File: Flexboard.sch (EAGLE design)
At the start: 421 parts, among them U1 MK22FX512AVLQ12

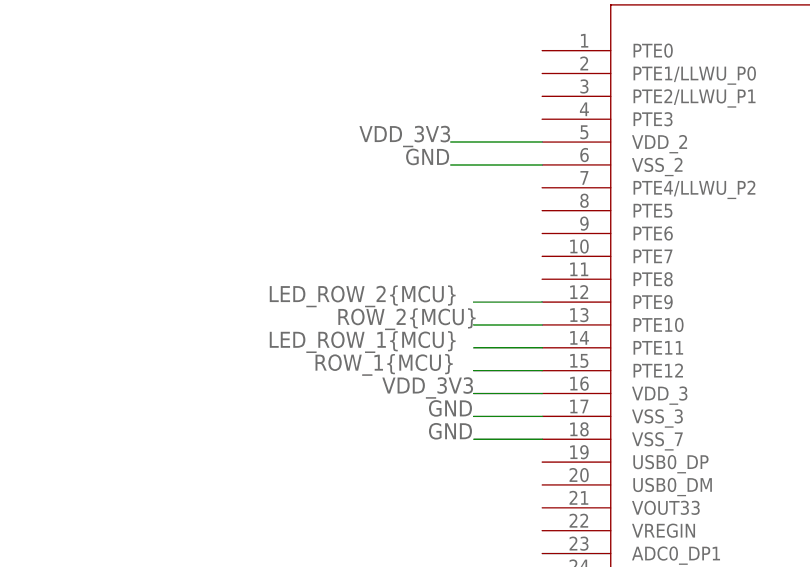
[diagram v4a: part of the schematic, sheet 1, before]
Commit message: All column and row traces routed to MCU
All column and row traces are connected to the MCU
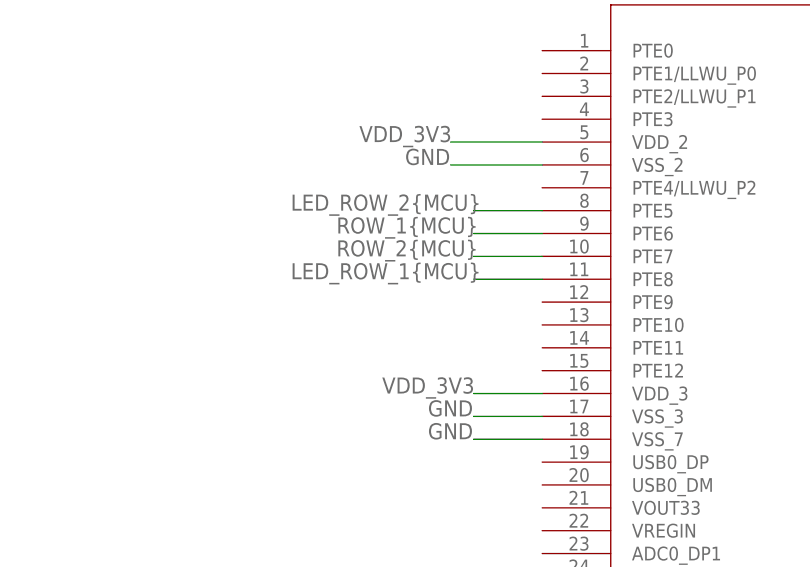
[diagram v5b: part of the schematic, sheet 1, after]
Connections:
- net LED_ROW_1{MCU}: now also U1A.PTE8; no longer U1A.PTE11
- net LED_ROW_2{MCU}: now also U1A.PTE5; no longer U1A.PTE9
- net ROW_1{MCU}: now also U1A.PTE6; no longer U1A.PTE12
- net ROW_2{MCU}: now also U1A.PTE7; no longer U1A.PTE10
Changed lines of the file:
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@@
 </segment>
 <segment>
-<pinref part="U1" gate="A" pin="PTE12"/>
-<wire x1="-48.26" y1="33.02" x2="-55.88" y2="33.02" width="0.1524" layer="91"/>
-<label x="-73.66" y="33.02" size="1.778" layer="95"/>
+<pinref part="U1" gate="A" pin="PTE6"/>
+<wire x1="-48.26" y1="48.26" x2="-55.88" y2="48.26" width="0.1524" layer="91"/>
+<label x="-71.12" y="48.26" size="1.778" layer="95"/>
 </segment>
 </net>
@@
 </segment>
 <segment>
-<pinref part="U1" gate="A" pin="PTE10"/>
-<wire x1="-48.26" y1="38.1" x2="-55.88" y2="38.1" width="0.1524" layer="91"/>
-<label x="-71.12" y="38.1" size="1.778" layer="95"/>
+<pinref part="U1" gate="A" pin="PTE7"/>
+<wire x1="-48.26" y1="45.72" x2="-55.88" y2="45.72" width="0.1524" layer="91"/>
+<label x="-71.12" y="45.72" size="1.778" layer="95"/>
 </segment>
 </net>
@@
 <net name="LED_ROW_2{MCU}" class="0">
 <segment>
-<pinref part="U1" gate="A" pin="PTE9"/>
-<wire x1="-48.26" y1="40.64" x2="-55.88" y2="40.64" width="0.1524" layer="91"/>
-<label x="-78.74" y="40.64" size="1.778" layer="95"/>
-</segment>
-<segment>
 <pinref part="SJ_MCU_LED_ROW2" gate="G$1" pin="2"/>
 <wire x1="58.42" y1="198.12" x2="66.04" y2="198.12" width="0.1524" layer="91"/>
 <label x="66.04" y="198.12" size="1.778" layer="95"/>
 </segment>
+<segment>
+<pinref part="U1" gate="A" pin="PTE5"/>
+<wire x1="-48.26" y1="50.8" x2="-55.88" y2="50.8" width="0.1524" layer="91"/>
+<label x="-76.2" y="50.8" size="1.778" layer="95"/>
+</segment>
 </net>
 <net name="LED_ROW_1{MCU}" class="0">
-<segment>
-<pinref part="U1" gate="A" pin="PTE11"/>
-<wire x1="-48.26" y1="35.56" x2="-55.88" y2="35.56" width="0.1524" layer="91"/>
-<label x="-78.74" y="35.56" size="1.778" layer="95"/>
-</segment>
 <segment>
 <pinref part="SJ_MCU_LED_ROW1" gate="G$1" pin="2"/>
@@
 <label x="66.04" y="205.74" size="1.778" layer="95"/>
 </segment>
+<segment>
+<pinref part="U1" gate="A" pin="PTE8"/>
+<wire x1="-48.26" y1="43.18" x2="-55.88" y2="43.18" width="0.1524" layer="91"/>
+<label x="-76.2" y="43.18" size="1.778" layer="95"/>
+</segment>
 </net>

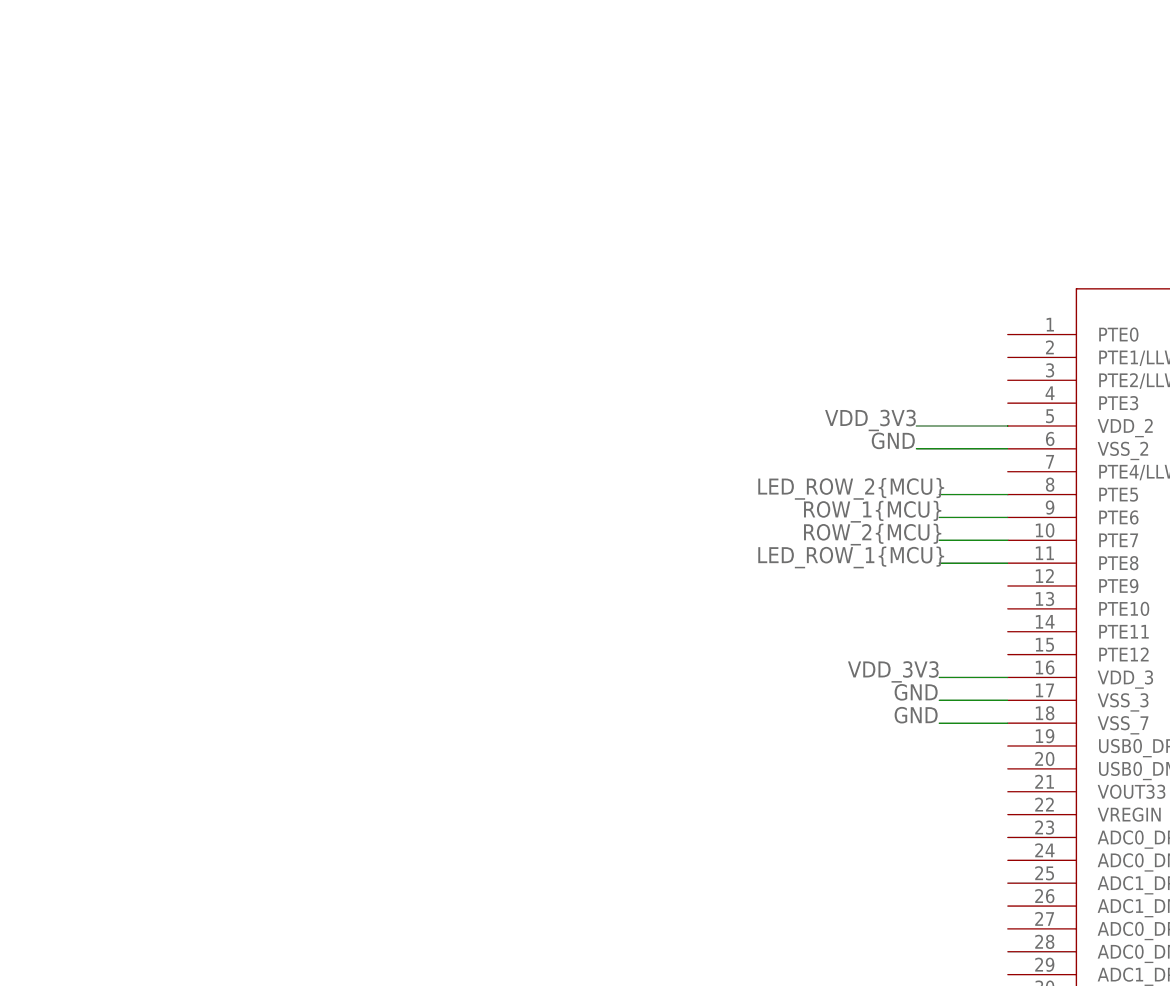
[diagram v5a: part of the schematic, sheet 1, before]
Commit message: Added usb to MCU and routed power planes
Added board wide power and ground planes, as well as USB traces to kinetis MCU.

Signed-off-by: Daniel DeGrasse <daniel@degrasse.com>
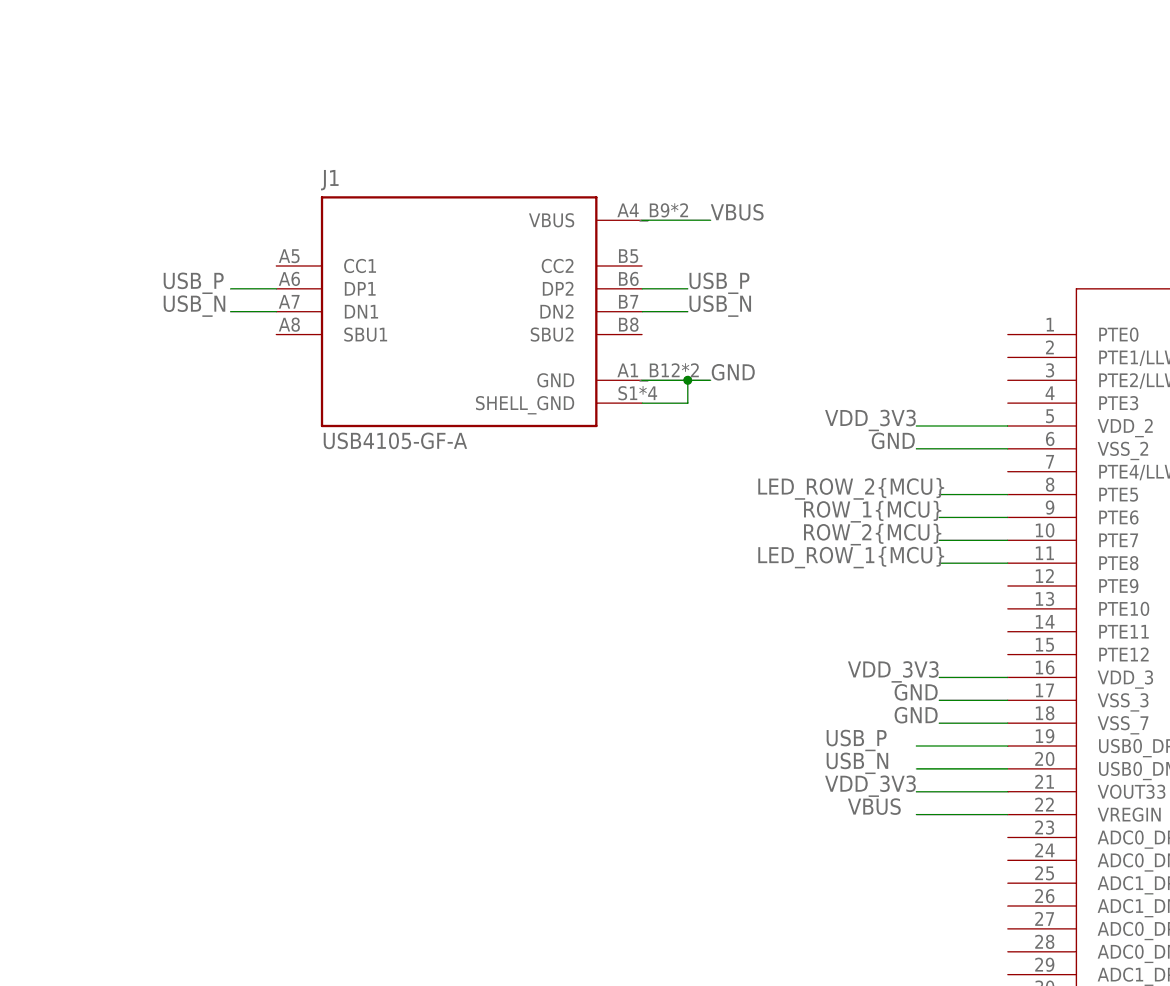
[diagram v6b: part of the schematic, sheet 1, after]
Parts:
- added J1: USB4105-GF-A, USB4105-GF-A:USB4105-GF-A
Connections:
- new net USB_N: J1.DN1, J1.DN2, U1A.USB0_DM
- new net USB_P: J1.DP1, J1.DP2, U1A.USB0_DP
- new net VBUS: J1.VBUS, U1A.VREGIN
- net GND: now also J1.GND, J1.SHELL_GND
- net VDD_3V3: now also U1A.VOUT33
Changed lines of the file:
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@@
 <part name="SJ_MCU_LED_COL23" library="SparkFun-Jumpers" deviceset="JUMPER-SMT_2_NC_TRACE" device="_NO-SILK" package3d_urn="urn:adsk.eagle:package:39286/1"/>
 <part name="SJ_MCU_LED_COL24" library="SparkFun-Jumpers" deviceset="JUMPER-SMT_2_NC_TRACE" device="_NO-SILK" package3d_urn="urn:adsk.eagle:package:39286/1"/>
+<part name="J1" library="USB4105-GF-A" deviceset="USB4105-GF-A" device=""/>
 </parts>
 <sheets>
@@
 <attribute name="NAME" x="-104.14" y="124.968" size="1.778" layer="95" font="vector" align="center"/>
 </instance>
+<instance part="J1" gate="G$1" x="-109.22" y="71.12" smashed="yes">
+<attribute name="NAME" x="-124.46" y="85.09" size="1.778" layer="95"/>
+<attribute name="VALUE" x="-124.46" y="55.88" size="1.778" layer="96"/>
+</instance>
 </instances>
 <busses>
@@
 <label x="101.6" y="-116.84" size="1.778" layer="95"/>
 </segment>
+<segment>
+<pinref part="U1" gate="A" pin="VOUT33"/>
+<wire x1="-48.26" y1="17.78" x2="-58.42" y2="17.78" width="0.1524" layer="91"/>
+<label x="-68.58" y="17.78" size="1.778" layer="95"/>
+</segment>
 </net>
 <net name="GND" class="0">
@@
 <label x="101.6" y="-119.38" size="1.778" layer="95"/>
 </segment>
+<segment>
+<pinref part="J1" gate="G$1" pin="GND"/>
+<wire x1="-88.9" y1="63.5" x2="-83.82" y2="63.5" width="0.1524" layer="91"/>
+<pinref part="J1" gate="G$1" pin="SHELL_GND"/>
+<wire x1="-83.82" y1="63.5" x2="-81.28" y2="63.5" width="0.1524" layer="91"/>
+<wire x1="-88.9" y1="60.96" x2="-83.82" y2="60.96" width="0.1524" layer="91"/>
+<wire x1="-83.82" y1="60.96" x2="-83.82" y2="63.5" width="0.1524" layer="91"/>
+<junction x="-83.82" y="63.5"/>
+<label x="-81.28" y="63.5" size="1.778" layer="95"/>
+</segment>
 </net>
 <net name="ROW_5{SB}" class="0">
@@
 </segment>
 </net>
+<net name="USB_P" class="0">
+<segment>
+<pinref part="U1" gate="A" pin="USB0_DP"/>
+<wire x1="-48.26" y1="22.86" x2="-58.42" y2="22.86" width="0.1524" layer="91"/>
+<label x="-68.58" y="22.86" size="1.778" layer="95"/>
+</segment>
+<segment>
+<pinref part="J1" gate="G$1" pin="DP2"/>
+<wire x1="-88.9" y1="73.66" x2="-83.82" y2="73.66" width="0.1524" layer="91"/>
+<label x="-83.82" y="73.66" size="1.778" layer="95"/>
+</segment>
+<segment>
+<pinref part="J1" gate="G$1" pin="DP1"/>
+<wire x1="-129.54" y1="73.66" x2="-134.62" y2="73.66" width="0.1524" layer="91"/>
+<label x="-142.24" y="73.66" size="1.778" layer="95"/>
+</segment>
+</net>
+<net name="USB_N" class="0">
+<segment>
+<pinref part="U1" gate="A" pin="USB0_DM"/>
+<wire x1="-48.26" y1="20.32" x2="-58.42" y2="20.32" width="0.1524" layer="91"/>
+<label x="-68.58" y="20.32" size="1.778" layer="95"/>
+</segment>
+<segment>
+<pinref part="J1" gate="G$1" pin="DN2"/>
+<wire x1="-88.9" y1="71.12" x2="-83.82" y2="71.12" width="0.1524" layer="91"/>
+<label x="-83.82" y="71.12" size="1.778" layer="95"/>
+</segment>
+<segment>
+<pinref part="J1" gate="G$1" pin="DN1"/>
+<wire x1="-129.54" y1="71.12" x2="-134.62" y2="71.12" width="0.1524" layer="91"/>
+<label x="-142.24" y="71.12" size="1.778" layer="95"/>
+</segment>
+</net>
+<net name="VBUS" class="0">
+<segment>
+<pinref part="U1" gate="A" pin="VREGIN"/>
+<wire x1="-48.26" y1="15.24" x2="-58.42" y2="15.24" width="0.1524" layer="91"/>
+<label x="-66.04" y="15.24" size="1.778" layer="95"/>
+</segment>
+<segment>
+<pinref part="J1" gate="G$1" pin="VBUS"/>
+<wire x1="-88.9" y1="81.28" x2="-81.28" y2="81.28" width="0.1524" layer="91"/>
+<label x="-81.28" y="81.28" size="1.778" layer="95"/>
+</segment>
+</net>

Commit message: Added decoupling capacitors around the mcu
added power caps to MCU, 1uF and 100nF

Signed-off-by: Daniel DeGrasse <daniel@degrasse.com>
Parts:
- added C1: 1000pF, C1206C102K1RACAUTO:C1206C102K1RACAUTO
- added C2, C3, C4, C8: 1uF, GCM31MR71H105KA55L:GCM31MR71H105KA55L
- added C5, C6, C7, C9: 100nF, C1206C104K5RAC7800:C1206C104K5RAC7800
- added R1: 10k, CRGCQ1206J10K:CRGCQ1206J10K
- added SW1: 1825910-7, 1825910-7:1825910-7
- added U$1: GRPB052VWQS-RC, GRPB052VWQS-RC:GRPB052VWQS-RC
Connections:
- removed net JTAG_TRST: U1A.PTA5
- new net EXTAL: U1A.PTA18
- new net EXTAL32: U1A.EXTAL32
- new net NMI: U1A.PTA4/LLWU_P3
- new net XTAL: U1B.PTA19
- new net XTAL32: U1A.XTAL32
- net COL_18{MCU}: now also U1A.PTA14; no longer U1A.PTA13/LLWU_P4
- net COL_19{MCU}: now also U1A.PTA12; no longer U1A.PTA11
- net COL_20{MCU}: now also U1A.PTA10; no longer U1A.PTA9
- net COL_21{MCU}: now also U1A.PTA8; no longer U1A.PTA7
- net COL_22{MCU}: now also U1A.PTA6; no longer U1A.PTA4/LLWU_P3
- net GND: now also C1.2, C2.2, C3.2, C4.2, C5.1, C6.1, C7.1, C8.2, C9.1, SW1.3, SW1.4, U$1.GND, U$1.GND2, U1A.VREFL, U1A.VSSA
- net JTAG_TCLK/SWD_CLK: now also U$1.TCK
- net JTAG_TDI: now also U$1.TDI
- net JTAG_TDO/TRACE_SWO: now also U$1.TDO
- net JTAG_TMS/SWD_DIO: now also U$1.TMS
- net LED_COL_18{MCU}: now also U1A.PTA13/LLWU_P4; no longer U1A.PTA12
- net LED_COL_19{MCU}: now also U1A.PTA11; no longer U1A.PTA10
- net LED_COL_20{MCU}: now also U1A.PTA9; no longer U1A.PTA8
- net LED_COL_21{MCU}: now also U1A.PTA7; no longer U1A.PTA6
- net RESET: now also C1.1, R1.1, SW1.1, SW1.2, U$1.NRESET
- net VDD_3V3: now also C2.1, C3.1, C4.1, C5.2, C6.2, C7.2, C8.1, C9.2, R1.2, U$1.VCC, U1A.VBAT, U1A.VDDA, U1A.VREFH
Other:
- note added: "JTAG"
- note added: "MCU"
- note added: "Solder Bridges"
- note added: "USB"

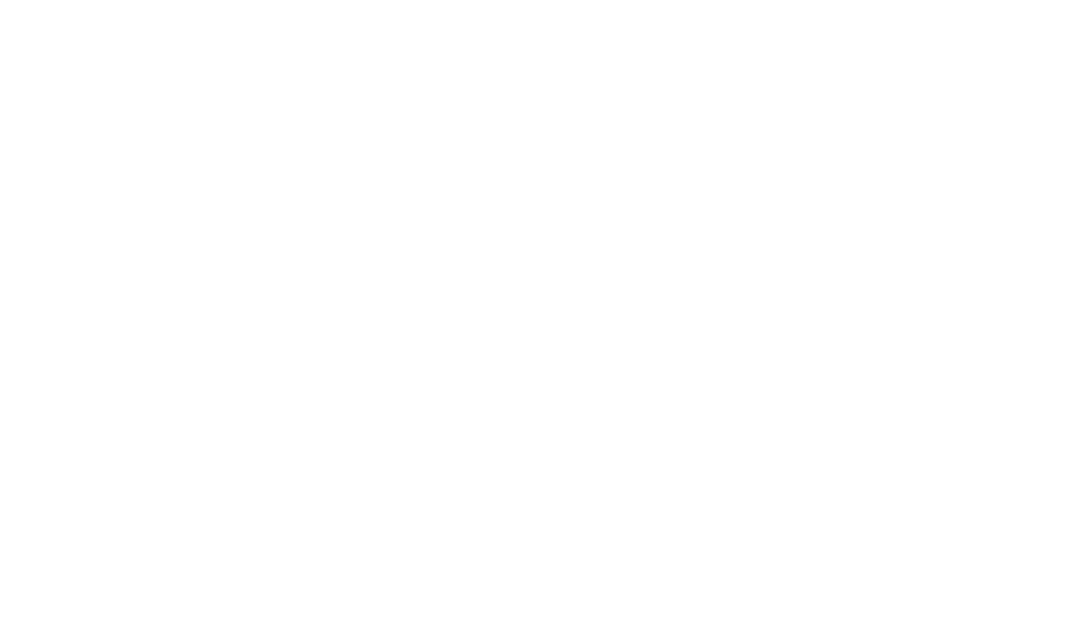
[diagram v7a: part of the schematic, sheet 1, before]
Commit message: added oscillators to design
added 8MHz and 32KHz crystals to design. Still need to add capacitors
and resistors for USB 5V as well as DP/DN

Signed-off-by: Daniel DeGrasse <daniel@degrasse.com>
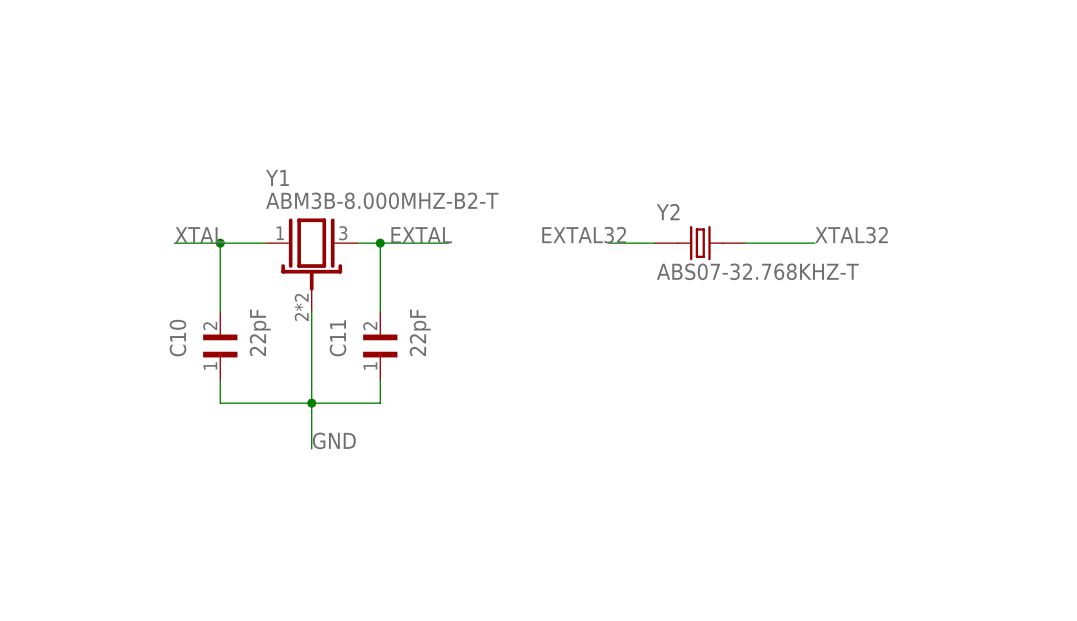
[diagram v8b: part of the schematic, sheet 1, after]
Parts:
- added C10, C11: 22pF, C1206C220JGGAC7800:C1206C220JGGAC7800
- added Y1: ABM3B-8.000MHZ-B2-T, ABM3B-8.000MHZ-B2-T:ABM3B-8.000MHZ-B2-T
- added Y2: ABS07-32.768KHZ-T, ABS07-32.768KHZ-T:ABS07-32.768KHZ-T
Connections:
- net EXTAL: now also C11.2, Y1.3
- net EXTAL32: now also Y2.1
- net GND: now also C10.1, C11.1, Y1.GND
- net XTAL: now also C10.2, Y1.1
- net XTAL32: now also Y2.2
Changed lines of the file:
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@@
 <part name="C8" library="GCM31MR71H105KA55L" deviceset="GCM31MR71H105KA55L" device="" value="1uF"/>
 <part name="C9" library="C1206C104K5RAC7800" deviceset="C1206C104K5RAC7800" device="" value="100nF"/>
+<part name="Y1" library="ABM3B-8.000MHZ-B2-T" deviceset="ABM3B-8.000MHZ-B2-T" device=""/>
+<part name="C10" library="C1206C220JGGAC7800" deviceset="C1206C220JGGAC7800" device="" value="22pF"/>
+<part name="C11" library="C1206C220JGGAC7800" deviceset="C1206C220JGGAC7800" device="" value="22pF"/>
+<part name="Y2" library="ABS07-32.768KHZ-T" deviceset="ABS07-32.768KHZ-T" device=""/>
 </parts>
 <sheets>
@@
 <attribute name="NAME" x="102.86906875" y="116.84" size="1.77843125" layer="95" rot="R90"/>
 <attribute name="VALUE" x="111.76848125" y="116.84" size="1.78096875" layer="96" rot="R90"/>
+</instance>
+<instance part="Y1" gate="G$1" x="220.98" y="15.24" smashed="yes">
+<attribute name="NAME" x="215.9" y="21.59" size="1.78073125" layer="95"/>
+<attribute name="VALUE" x="215.9" y="19.05" size="1.78303125" layer="96"/>
+</instance>
+<instance part="C10" gate="G$1" x="210.82" y="2.54" smashed="yes" rot="R90">
+<attribute name="NAME" x="207.00906875" y="2.54" size="1.77843125" layer="95" rot="R90"/>
+<attribute name="VALUE" x="215.90848125" y="2.54" size="1.78096875" layer="96" rot="R90"/>
+</instance>
+<instance part="C11" gate="G$1" x="228.6" y="2.54" smashed="yes" rot="R90">
+<attribute name="NAME" x="224.78906875" y="2.54" size="1.77843125" layer="95" rot="R90"/>
+<attribute name="VALUE" x="233.68848125" y="2.54" size="1.78096875" layer="96" rot="R90"/>
+</instance>
+<instance part="Y2" gate="G$1" x="264.16" y="15.24" smashed="yes">
+<attribute name="NAME" x="259.325690625" y="17.78436875" size="1.781059375" layer="95"/>
+<attribute name="VALUE" x="259.323540625" y="11.167190625" size="1.78185" layer="96"/>
 </instance>
 </instances>
@@
 <junction x="93.98" y="109.22"/>
 </segment>
+<segment>
+<pinref part="C10" gate="G$1" pin="1"/>
+<wire x1="210.82" y1="0" x2="210.82" y2="-2.54" width="0.1524" layer="91"/>
+<wire x1="210.82" y1="-2.54" x2="220.98" y2="-2.54" width="0.1524" layer="91"/>
+<pinref part="C11" gate="G$1" pin="1"/>
+<wire x1="220.98" y1="-2.54" x2="228.6" y2="-2.54" width="0.1524" layer="91"/>
+<wire x1="228.6" y1="-2.54" x2="228.6" y2="0" width="0.1524" layer="91"/>
+<pinref part="Y1" gate="G$1" pin="GND"/>
+<wire x1="220.98" y1="7.62" x2="220.98" y2="-2.54" width="0.1524" layer="91"/>
+<junction x="220.98" y="-2.54"/>
+<wire x1="220.98" y1="-2.54" x2="220.98" y2="-7.62" width="0.1524" layer="91"/>
+<label x="220.98" y="-7.62" size="1.778" layer="95"/>
+</segment>
 </net>
 <net name="ROW_5{SB}" class="0">
@@
 <label x="144.78" y="-10.16" size="1.778" layer="95"/>
 </segment>
+<segment>
+<pinref part="Y2" gate="G$1" pin="1"/>
+<wire x1="259.08" y1="15.24" x2="254" y2="15.24" width="0.1524" layer="91"/>
+<label x="246.38" y="15.24" size="1.778" layer="95"/>
+</segment>
 </net>
 <net name="XTAL32" class="0">
@@
 <label x="144.78" y="-12.7" size="1.778" layer="95"/>
 </segment>
+<segment>
+<pinref part="Y2" gate="G$1" pin="2"/>
+<wire x1="269.24" y1="15.24" x2="276.86" y2="15.24" width="0.1524" layer="91"/>
+<label x="276.86" y="15.24" size="1.778" layer="95"/>
+</segment>
 </net>
 <net name="EXTAL" class="0">
@@
 <label x="144.78" y="68.58" size="1.778" layer="95"/>
 </segment>
+<segment>
+<pinref part="Y1" gate="G$1" pin="3"/>
+<wire x1="226.06" y1="15.24" x2="228.6" y2="15.24" width="0.1524" layer="91"/>
+<label x="229.616" y="15.24" size="1.778" layer="95"/>
+<pinref part="C11" gate="G$1" pin="2"/>
+<wire x1="228.6" y1="15.24" x2="236.22" y2="15.24" width="0.1524" layer="91"/>
+<wire x1="228.6" y1="7.62" x2="228.6" y2="15.24" width="0.1524" layer="91"/>
+<junction x="228.6" y="15.24"/>
+</segment>
 </net>
 <net name="XTAL" class="0">
@@
 <label x="-15.24" y="-60.96" size="1.778" layer="95"/>
 </segment>
-</net>
+<segment>
+<pinref part="Y1" gate="G$1" pin="1"/>
+<wire x1="215.9" y1="15.24" x2="210.82" y2="15.24" width="0.1524" layer="91"/>
+<label x="205.74" y="15.24" size="1.778" layer="95"/>
+<pinref part="C10" gate="G$1" pin="2"/>
+<wire x1="210.82" y1="15.24" x2="205.74" y2="15.24" width="0.1524" layer="91"/>
+<wire x1="210.82" y1="7.62" x2="210.82" y2="15.24" width="0.1524" layer="91"/>
+<junction x="210.82" y="15.24"/>
+</segment>
+</net>
